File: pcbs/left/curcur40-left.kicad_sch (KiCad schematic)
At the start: 79 parts, among them J1 TYPE-C-31-M-13C, J2 TRS, J4 Conn_01x03, SW1 SW_Push, SW10 SW_Push, SW11 SW_Push, SW12 SW_Push, SW13 SW_Push, SW14 SW_Push, SW15 SW_Push, SW16 SW_Push, SW17 SW_Push, SW18 SW_Push, SW2 SW_Push, SW3 SW_Push, SW4 SW_Push, SW5 SW_Push, SW6 SW_Push, SW7 SW_Push, SW8 SW_Push, SW9 SW_Push, U1 RP2040, U2 NCP1117LPST33T3G, U3 TPD4E05U06DQAR, U4 W25Q128JVSIQ, Y1 12MHz 18pF

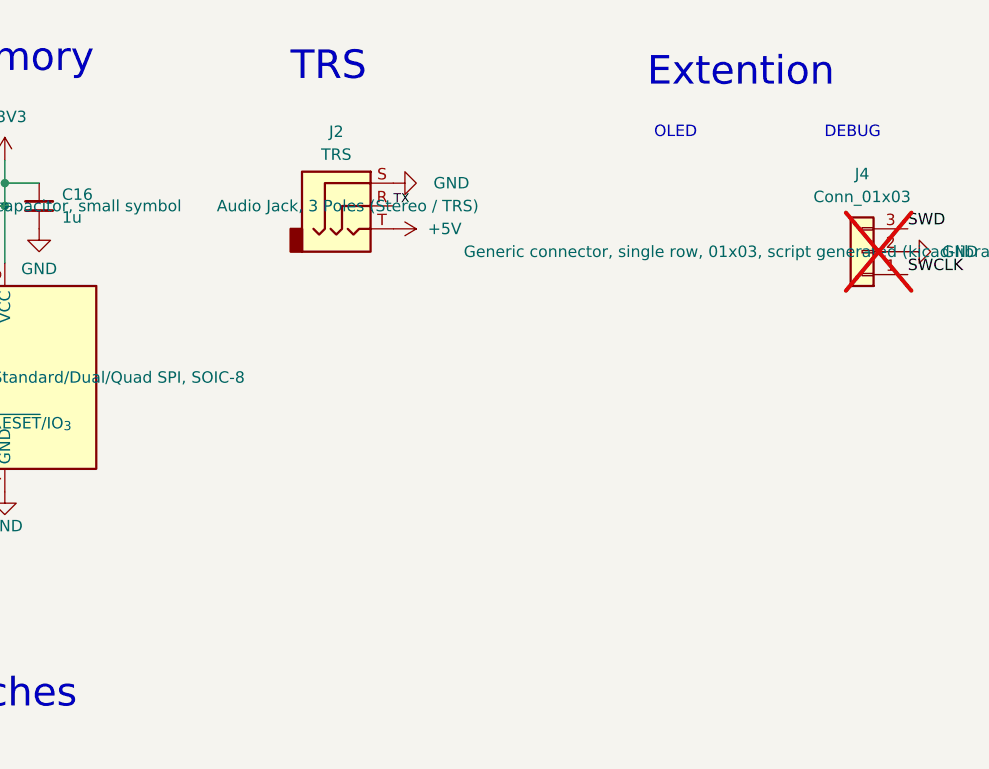
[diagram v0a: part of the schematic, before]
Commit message: feat(pcb): replace split TRRS jack with USB-C receptacle and ESD/series protection
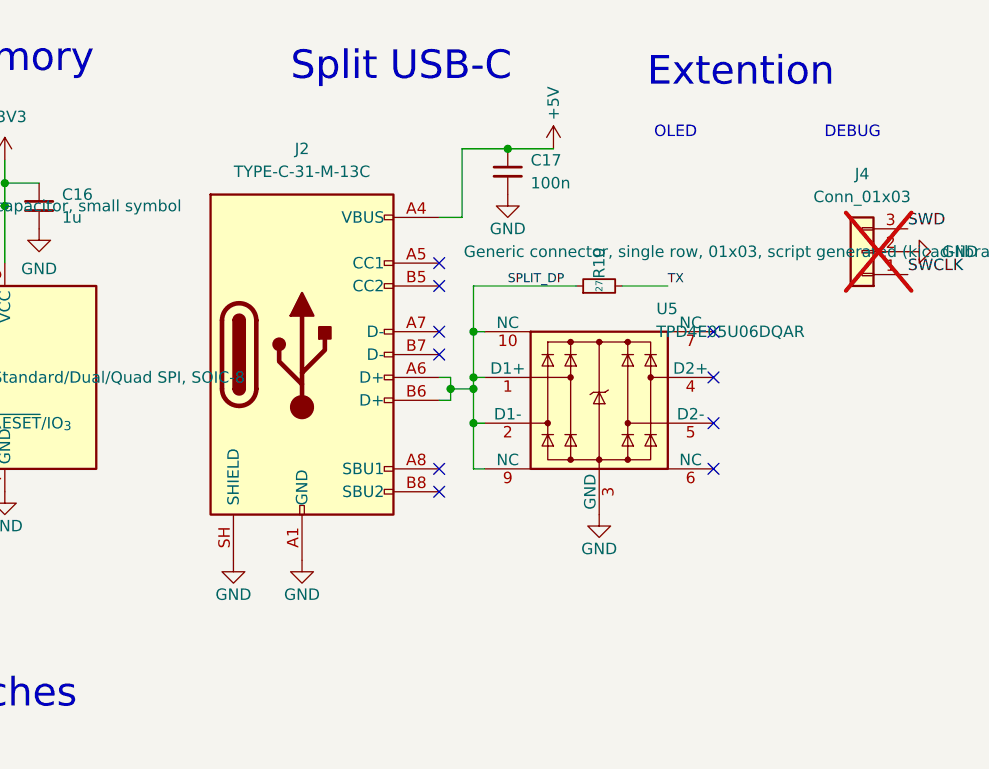
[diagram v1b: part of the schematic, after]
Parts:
- added C17: 100n, Capacitor_SMD:C_0402_1005Metric, symbol Device:C_Small
- added R10: 27, Resistor_SMD:R_0402_1005Metric, symbol Device:R_Small
- added U5: TPD4E05U06DQAR, Package_SON:USON-10_2.5x1.0mm_P0.5mm, symbol Power_Protection:TPD4EUSB30
- J2: value TRS -> TYPE-C-31-M-13C; footprint kbd:Jack_PJ-398A-5A_PJ-399B-6A -> kbd:USB_C_Receptacle_TYPE-C-31-M-13C; symbol Connector_Audio:AudioJack3 -> Connector:USB_C_Receptacle_USB2.0_16P; JLCPCB Part # C128994 -> C2848620
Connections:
- net +5V: now also J2.A4 (VBUS), J2.A9 (VBUS), J2.B4 (VBUS), J2.B9 (VBUS), C17.1; no longer J2.T
- net GND: now also J2.A1 (GND), J2.A12 (GND), J2.B1 (GND), J2.B12 (GND), J2.SH (SHIELD), C17.2, U5.3 (GND), U5.8 (GND); no longer J2.S
- net TX: now also R10.2; no longer J2.R
- new net SPLIT_DP: J2.A6 (D+), J2.B6 (D+), R10.1, U5.1 (D1+), U5.10 (NC), U5.2 (D1-), U5.9 (NC)
- no-connect marks 8 -> 18
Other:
- note added: "Split USB-C"
- note removed: "TRS"
